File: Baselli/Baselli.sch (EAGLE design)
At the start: 34 parts, among them J2 DF12-ELLI-HEADER-TOP, J3 DF12-ELLI-RECEPTABLE-BOTTOM, J4 FTDI-SER-6-PP, U1 LCMXO2-256HC-4SG32, U2 STM32F051R

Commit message: Change JTAG connector and PIN order for STM32F PB1, PB4 and PB8
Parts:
- removed JP1: (no value), SparkFun-Connectors:M08
- added J5: JTAG_PROG, ELL-i-Connectors:JTAG_PROG
- added Q1: MOSFET-PCHANNELIRLML2244, SparkFun-DiscreteSemi:MOSFET-PCHANNELIRLML2244
- added R12, R13, R14: NP, ELL-i-Passives:R0402
- added R4: 47K, ELL-i-Passives:R0402
- added R9: 10K, ELL-i-Passives:R0402
- R8: value 4K7 (NP) -> 10K
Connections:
- net D3MCU renamed PA11-D3MCU
- net D8MCU renamed PB7-D8MCU
- net N$13 renamed PB10
- net N$14 renamed PB11
- net N$4 renamed PF4
- net N$5 renamed PF5
- removed net N$7: SW1.13, U2PDF.PF6
- removed net N$8: SW1.14, U2PDF.PF7
- new net +5V: J2.5V, J3.5V
- new net N$1: J5.3, Q1.G, R4.2
- new net N$6: J5.7, R14.2
- new net PF6: R13.2, SW1.13, U2PDF.PF6
- new net PF7: R12.2, SW1.14, U2PDF.PF7
- new net VIN: J2.VIN, J3.VIN
- net +3V3: now also J2.VCC(IO), J3.VCC(IO), J5.1, Q1.S, R12.1, R4.1, R9.1; no longer JP1.8
- net D10: now also J5.6; no longer JP1.5
- net D5: now also U2PB.PB1-ADC_IN9; no longer U2PB.PB4
- net D7: now also U2PB.PB8; no longer U2PB.PB1-ADC_IN9
- net GNDI: now also J5.5, J5.9, R13.1, R14.1; no longer JP1.1
- net JTAGENB: now also Q1.D, U2PB.PB4; no longer JP1.6, U2PB.PB8
- net JTDI: now also J5.8; no longer JP1.4
- net NRES: now also J5.10; no longer JP1.7
- net SWCLK: now also J5.4; no longer JP1.3
- net SWDIO: now also J5.2, R9.2; no longer JP1.2
- net VDDA: now also J2.AREF, J3.AREF
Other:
- note added: "In STM32F072 TQFP100, PF6 and PF7 pins are used for GND and VCCIO"
- note removed: "PLACEHOLDER"
- moved on the sheet: R34, R35, R5, R6, R7, R8, SW1, SW2, U1ERB, U1IO, U2PA, U2PB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

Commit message: Adding WS2812B to Baselli board schematics
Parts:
- added D1: (no value), SparkFun-LED:WS2812B
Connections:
- new net PA7: D1.DIN, U2PA.PA7-ADC_IN7
- net +5V: now also D1.VDD
- net GNDI: now also D1.VSS
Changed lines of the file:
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@@
 <?xml version="1.0" encoding="utf-8"?>
 <!DOCTYPE eagle SYSTEM "eagle.dtd">
-<eagle version="6.5.2">
+<eagle version="6.5.0">
 <drawing>
 <settings>
@@
 <part name="R13" library="ELL-i-Passives" deviceset="R" device="0402" value="NP"/>
 <part name="R14" library="ELL-i-Passives" deviceset="R" device="0402" value="NP"/>
+<part name="D1" library="SparkFun-LED" deviceset="WS2812B" device=""/>
+<part name="GNDI15" library="supply1" deviceset="GNDI" device=""/>
+<part name="P+2" library="supply1" deviceset="+5V" device=""/>
 </parts>
 <sheets>
@@
 <instance part="R13" gate="G$1" x="33.02" y="58.42"/>
 <instance part="R14" gate="G$1" x="261.62" y="55.88" rot="R90"/>
+<instance part="D1" gate="G$1" x="-76.2" y="50.8"/>
+<instance part="GNDI15" gate="G$1" x="-53.34" y="43.18"/>
+<instance part="P+2" gate="1" x="-88.9" y="63.5"/>
 </instances>
 <busses>
@@
 <wire x1="15.24" y1="58.42" x2="27.94" y2="58.42" width="0.1524" layer="91"/>
 </segment>
+<segment>
+<pinref part="D1" gate="G$1" pin="VSS"/>
+<pinref part="GNDI15" gate="G$1" pin="GNDI"/>
+<wire x1="-58.42" y1="48.26" x2="-53.34" y2="48.26" width="0.1524" layer="91"/>
+<wire x1="-53.34" y1="48.26" x2="-53.34" y2="45.72" width="0.1524" layer="91"/>
+</segment>
 </net>
 <net name="A0" class="0">
@@
 <label x="91.44" y="325.12" size="1.778" layer="95" xref="yes"/>
 </segment>
+<segment>
+<pinref part="D1" gate="G$1" pin="VDD"/>
+<wire x1="-81.28" y1="55.88" x2="-88.9" y2="55.88" width="0.1524" layer="91"/>
+<wire x1="-88.9" y1="55.88" x2="-88.9" y2="60.96" width="0.1524" layer="91"/>
+<pinref part="P+2" gate="1" pin="+5V"/>
+</segment>
 </net>
 <net name="VIN" class="0">
@@
 </segment>
 </net>
+<net name="PA7" class="0">
+<segment>
+<pinref part="U2" gate="PA" pin="PA7-ADC_IN7"/>
+<wire x1="73.66" y1="154.94" x2="86.36" y2="154.94" width="0.1524" layer="91"/>
+<label x="83.82" y="154.94" size="1.27" layer="95"/>
+</segment>
+<segment>
+<pinref part="D1" gate="G$1" pin="DIN"/>
+<wire x1="-58.42" y1="55.88" x2="-50.8" y2="55.88" width="0.1524" layer="91"/>
+<label x="-53.34" y="55.88" size="1.27" layer="95"/>
+</segment>
+</net>

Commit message: Adding WS2812B RGB LED to Baselli. Begining Arduelli schematic
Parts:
- added TP1: TEST_POINT-5000, ELL-i-Passives:TEST_POINT-5000
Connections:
- new net N$2: D1.DOUT, TP1.P$1
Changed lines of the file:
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@@
 <part name="GNDI15" library="supply1" deviceset="GNDI" device=""/>
 <part name="P+2" library="supply1" deviceset="+5V" device=""/>
+<part name="TP1" library="ELL-i-Passives" deviceset="TEST_POINT" device="-5000"/>
 </parts>
 <sheets>
@@
 <instance part="GNDI15" gate="G$1" x="-53.34" y="43.18"/>
 <instance part="P+2" gate="1" x="-88.9" y="63.5"/>
+<instance part="TP1" gate="TP$1" x="-88.9" y="45.72"/>
 </instances>
 <busses>
@@
 </segment>
 </net>
-<net name="+5V" class="0">
+<net name="+5V" class="1">
 <segment>
 <pinref part="J3" gate="E" pin="5V"/>
@@
 <net name="PA7" class="0">
 <segment>
-<pinref part="U2" gate="PA" pin="PA7-ADC_IN7"/>
-<wire x1="73.66" y1="154.94" x2="86.36" y2="154.94" width="0.1524" layer="91"/>
-<label x="83.82" y="154.94" size="1.27" layer="95"/>
-</segment>
-<segment>
 <pinref part="D1" gate="G$1" pin="DIN"/>
 <wire x1="-58.42" y1="55.88" x2="-50.8" y2="55.88" width="0.1524" layer="91"/>
-<label x="-53.34" y="55.88" size="1.27" layer="95"/>
-</segment>
-</net>
+<label x="-50.8" y="55.88" size="1.778" layer="95" xref="yes"/>
+</segment>
+<segment>
+<pinref part="U2" gate="PA" pin="PA7-ADC_IN7"/>
+<wire x1="73.66" y1="154.94" x2="76.2" y2="154.94" width="0.1524" layer="91"/>
+<label x="76.2" y="154.94" size="1.27" layer="95" xref="yes"/>
+</segment>
+</net>
+<net name="N$2" class="0">
+<segment>
+<pinref part="TP1" gate="TP$1" pin="P$1"/>
+<pinref part="D1" gate="G$1" pin="DOUT"/>
+<wire x1="-88.9" y1="48.26" x2="-81.28" y2="48.26" width="0.1524" layer="91"/>
+</segment>
+</net>

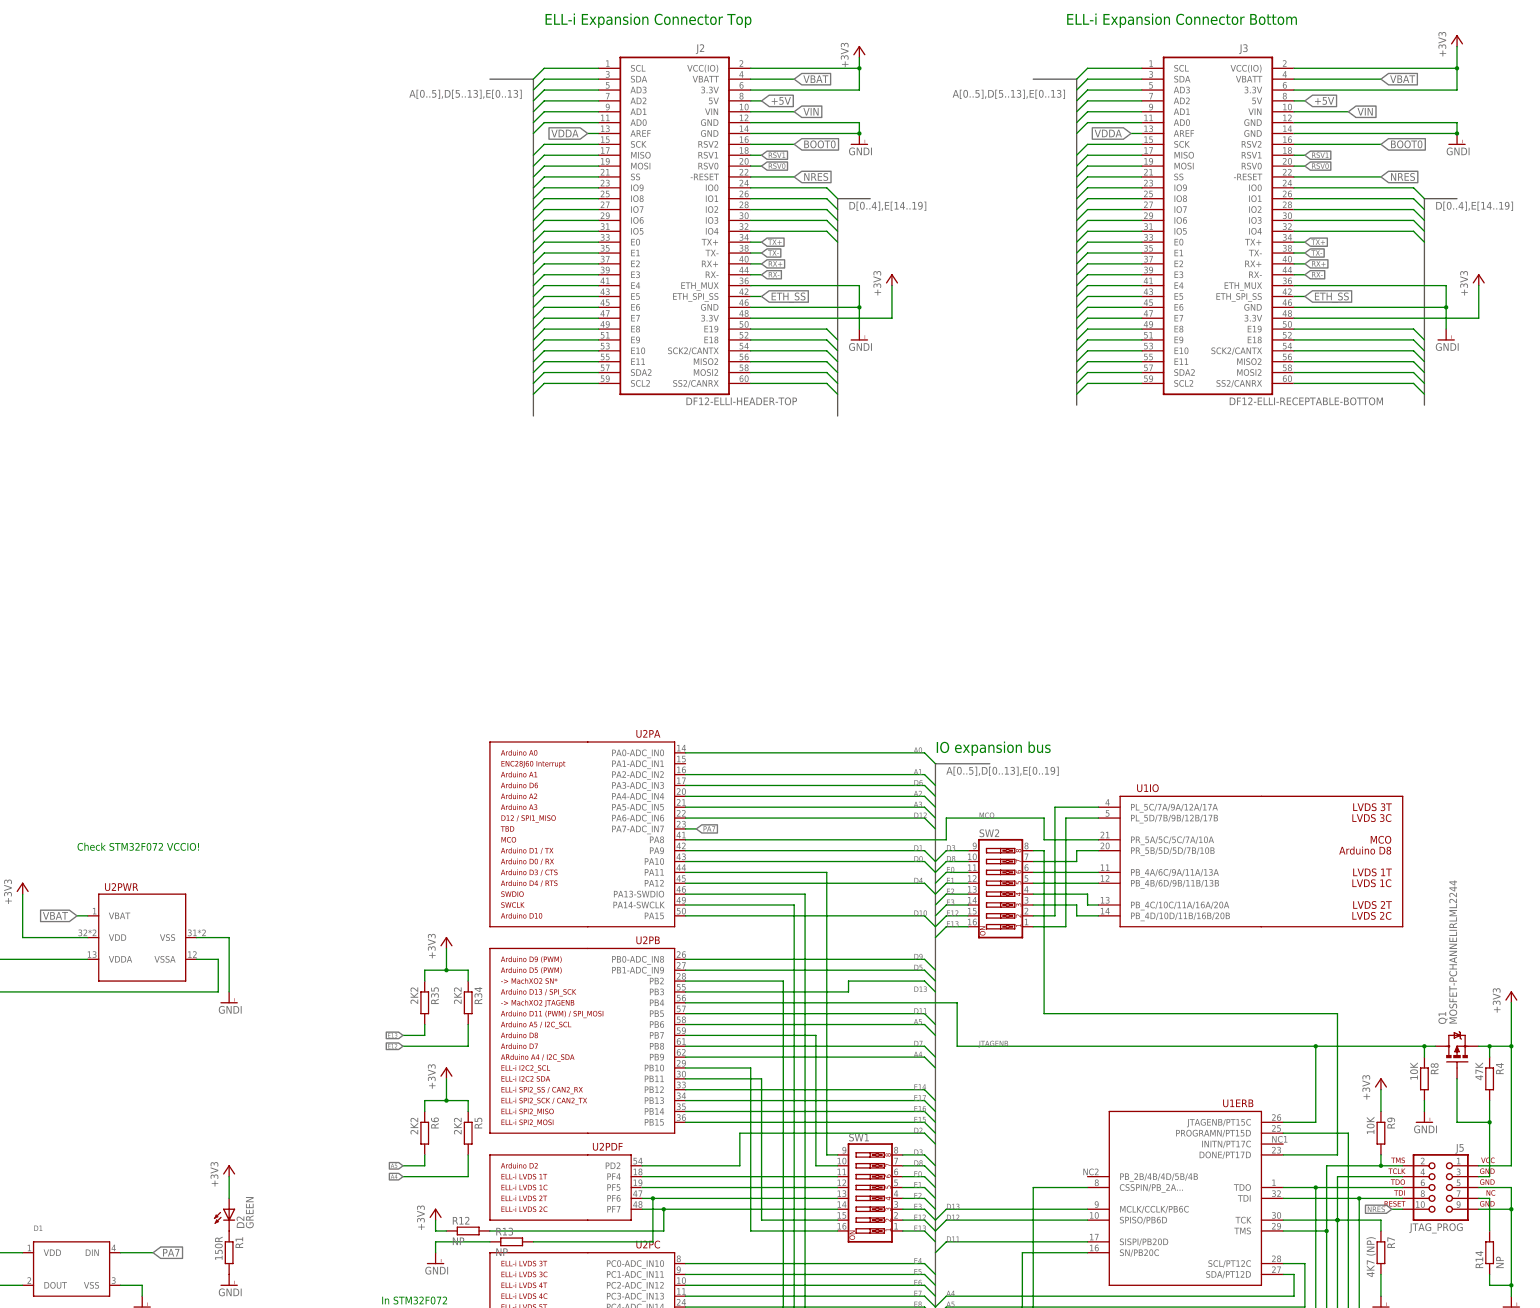
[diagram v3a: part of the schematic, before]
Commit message: Add resistors R10 and R11 to Baselli
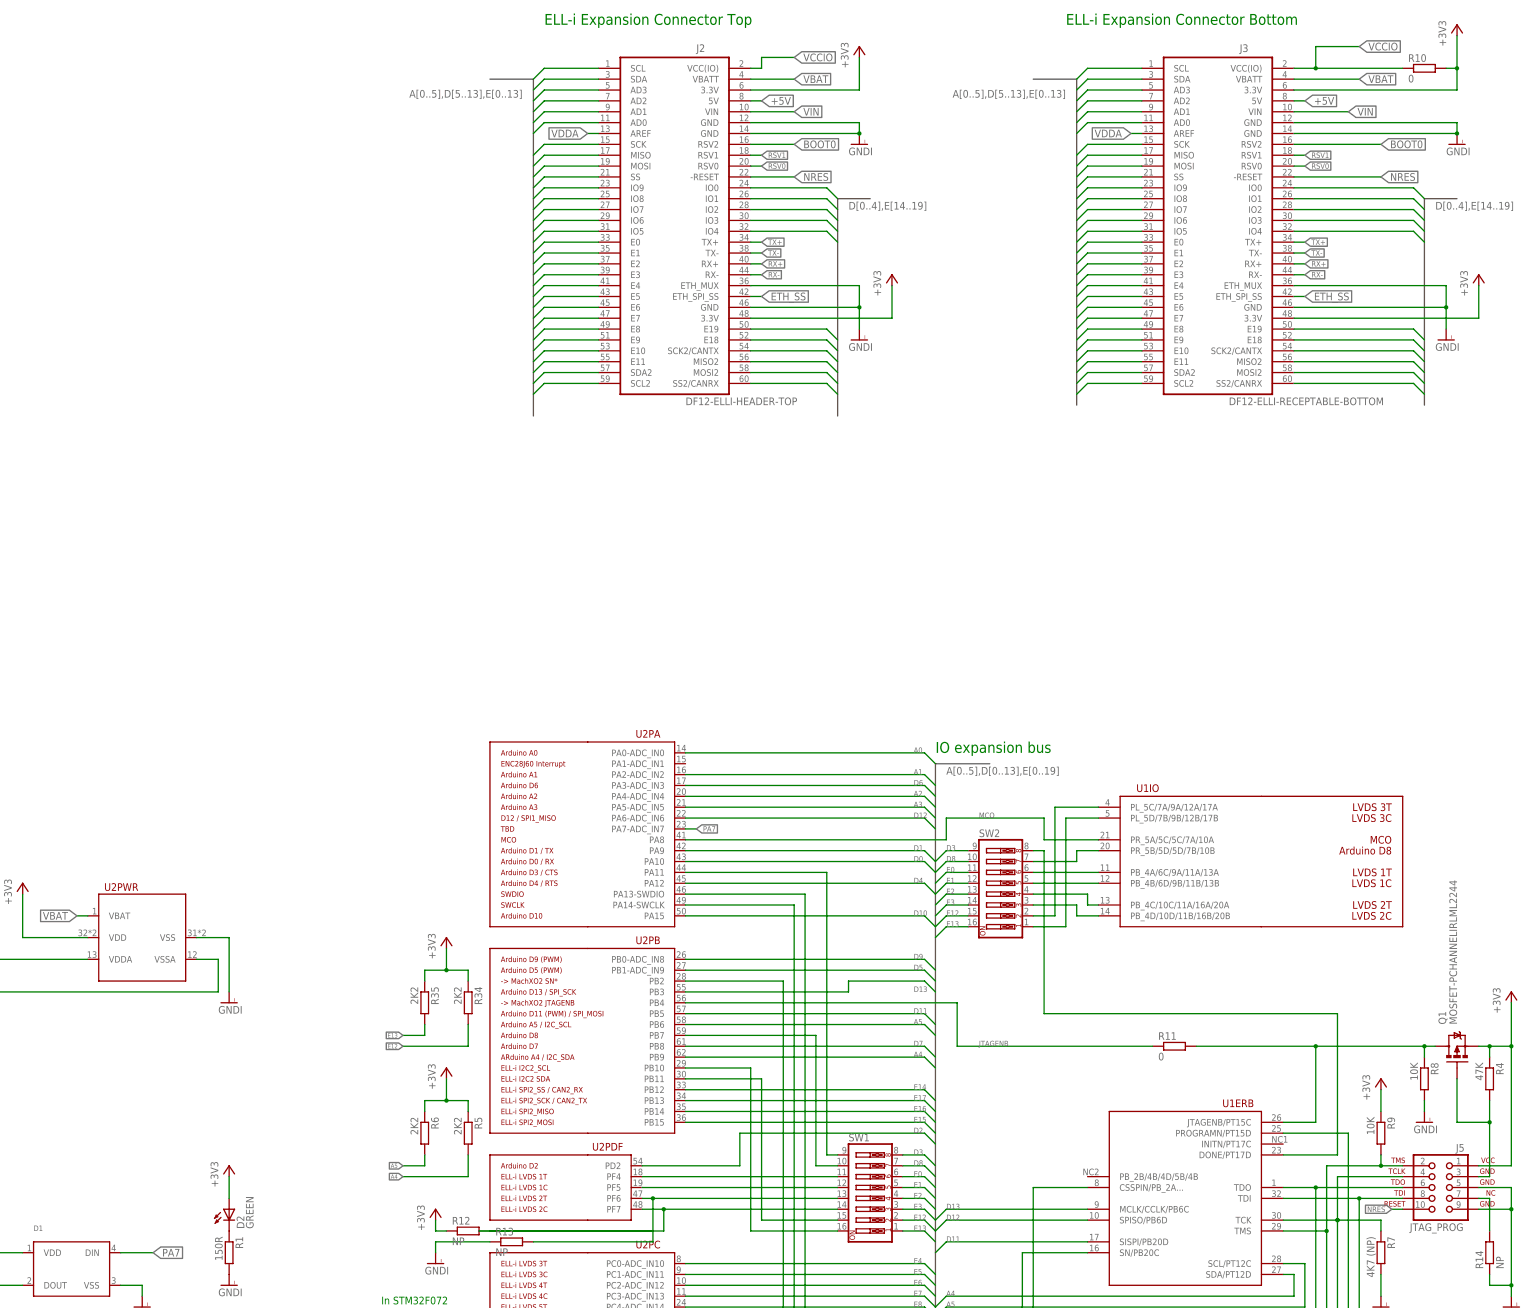
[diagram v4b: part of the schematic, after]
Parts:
- added R10: 0, ELL-i-Passives:R0402
- added R11: 0, ELL-i-Passives:R0805
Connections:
- net N$2 renamed DOUT
- new net JTAGENB$2: Q1.D, R11.2, R8.1, U1ERB.JTAGENB/PT15C
- new net VCCIO: J2.VCC(IO), J3.VCC(IO), R10.1
- net +3V3: now also R10.2; no longer J2.VCC(IO), J3.VCC(IO)
- net JTAGENB: now also R11.1; no longer Q1.D, R8.1, U1ERB.JTAGENB/PT15C
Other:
- note removed: "Check STM32F072 VCCIO!"
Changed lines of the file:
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@@
 <?xml version="1.0" encoding="utf-8"?>
 <!DOCTYPE eagle SYSTEM "eagle.dtd">
-<eagle version="6.5.0">
+<eagle version="6.5.2">
 <drawing>
 <settings>
@@
 <part name="P+2" library="supply1" deviceset="+5V" device=""/>
 <part name="TP1" library="ELL-i-Passives" deviceset="TEST_POINT" device="-5000"/>
+<part name="R10" library="ELL-i-Passives" deviceset="R" device="0402" value="0"/>
+<part name="R11" library="ELL-i-Passives" deviceset="R" device="0805" value="0"/>
 </parts>
 <sheets>
@@
 <text x="40.64" y="342.9" size="2.54" layer="91">ELL-i Expansion Connector Top</text>
 <text x="162.56" y="342.9" size="2.54" layer="91">ELL-i Expansion Connector Bottom</text>
-<text x="-68.58" y="149.86" size="1.778" layer="91">Check STM32F072 VCCIO!</text>
 <text x="-198.12" y="109.22" size="1.27" layer="91">A diode here?</text>
 <text x="2.54" y="30.48" size="1.778" layer="91">In STM32F072
@@
 <instance part="GNDI5" gate="G$1" x="-134.62" y="50.8"/>
 <instance part="+3V5" gate="G$1" x="114.3" y="337.82"/>
-<instance part="+3V8" gate="G$1" x="254" y="340.36"/>
+<instance part="+3V8" gate="G$1" x="254" y="342.9"/>
 <instance part="GNDI10" gate="G$1" x="114.3" y="314.96"/>
 <instance part="GNDI11" gate="G$1" x="254" y="314.96"/>
@@
 <instance part="P+2" gate="1" x="-88.9" y="63.5"/>
 <instance part="TP1" gate="TP$1" x="-88.9" y="45.72"/>
+<instance part="R10" gate="G$1" x="246.38" y="332.74"/>
+<instance part="R11" gate="G$1" x="187.96" y="104.14"/>
 </instances>
 <busses>
@@
 <segment>
 <pinref part="+3V8" gate="G$1" pin="+3V3"/>
-<wire x1="254" y1="337.82" x2="254" y2="332.74" width="0.1524" layer="91"/>
+<wire x1="254" y1="340.36" x2="254" y2="332.74" width="0.1524" layer="91"/>
 <wire x1="254" y1="332.74" x2="254" y2="327.66" width="0.1524" layer="91"/>
 <wire x1="254" y1="327.66" x2="215.9" y2="327.66" width="0.1524" layer="91"/>
 <pinref part="J3" gate="E" pin="3.3V@6"/>
-<pinref part="J3" gate="E" pin="VCC(IO)"/>
-<wire x1="215.9" y1="332.74" x2="254" y2="332.74" width="0.1524" layer="91"/>
+<pinref part="R10" gate="G$1" pin="2"/>
+<wire x1="251.46" y1="332.74" x2="254" y2="332.74" width="0.1524" layer="91"/>
 <junction x="254" y="332.74"/>
 </segment>
@@
 <pinref part="+3V5" gate="G$1" pin="+3V3"/>
 <pinref part="J2" gate="E" pin="3.3V@6"/>
-<wire x1="114.3" y1="335.28" x2="114.3" y2="332.74" width="0.1524" layer="91"/>
-<wire x1="114.3" y1="332.74" x2="114.3" y2="327.66" width="0.1524" layer="91"/>
+<wire x1="114.3" y1="335.28" x2="114.3" y2="327.66" width="0.1524" layer="91"/>
 <wire x1="114.3" y1="327.66" x2="88.9" y2="327.66" width="0.1524" layer="91"/>
-<pinref part="J2" gate="E" pin="VCC(IO)"/>
-<wire x1="114.3" y1="332.74" x2="88.9" y2="332.74" width="0.1524" layer="91"/>
-<junction x="114.3" y="332.74"/>
 </segment>
 <segment>
@@
 <net name="JTAGENB" class="0">
 <segment>
-<pinref part="U1" gate="ERB" pin="JTAGENB/PT15C"/>
-<wire x1="137.16" y1="104.14" x2="220.98" y2="104.14" width="0.1524" layer="91"/>
-<wire x1="220.98" y1="104.14" x2="220.98" y2="86.36" width="0.1524" layer="91"/>
-<wire x1="220.98" y1="86.36" x2="213.36" y2="86.36" width="0.1524" layer="91"/>
+<wire x1="137.16" y1="104.14" x2="182.88" y2="104.14" width="0.1524" layer="91"/>
 <label x="142.24" y="104.14" size="1.27" layer="95"/>
-<junction x="220.98" y="104.14"/>
-<wire x1="220.98" y1="104.14" x2="246.38" y2="104.14" width="0.1524" layer="91"/>
-<pinref part="Q1" gate="G$1" pin="D"/>
-<pinref part="R8" gate="G$1" pin="1"/>
-<wire x1="246.38" y1="104.14" x2="248.92" y2="104.14" width="0.1524" layer="91"/>
-<wire x1="246.38" y1="104.14" x2="246.38" y2="101.6" width="0.1524" layer="91"/>
-<junction x="246.38" y="104.14"/>
 <wire x1="137.16" y1="104.14" x2="137.16" y2="114.3" width="0.1524" layer="91"/>
 <pinref part="U2" gate="PB" pin="PB4"/>
 <wire x1="137.16" y1="114.3" x2="73.66" y2="114.3" width="0.1524" layer="91"/>
+<pinref part="R11" gate="G$1" pin="1"/>
 </segment>
 </net>
@@
 <segment>
 <pinref part="J3" gate="E" pin="VBATT"/>
-<wire x1="215.9" y1="330.2" x2="236.22" y2="330.2" width="0.1524" layer="91"/>
-<label x="236.22" y="330.2" size="1.778" layer="95" xref="yes"/>
+<wire x1="215.9" y1="330.2" x2="231.14" y2="330.2" width="0.1524" layer="91"/>
+<label x="231.14" y="330.2" size="1.778" layer="95" xref="yes"/>
 </segment>
 <segment>
@@
 <junction x="68.58" y="66.04"/>
 </segment>
+<segment>
+<wire x1="25.4" y1="60.96" x2="66.04" y2="60.96" width="0.1524" layer="91"/>
+</segment>
 </net>
 <net name="+5V" class="1">
@@
 </segment>
 </net>
-<net name="N$2" class="0">
+<net name="VCCIO" class="0">
+<segment>
+<pinref part="J2" gate="E" pin="VCC(IO)"/>
+<wire x1="88.9" y1="332.74" x2="91.44" y2="332.74" width="0.1524" layer="91"/>
+<wire x1="91.44" y1="332.74" x2="91.44" y2="335.28" width="0.1524" layer="91"/>
+<wire x1="91.44" y1="335.28" x2="99.06" y2="335.28" width="0.1524" layer="91"/>
+<label x="99.06" y="335.28" size="1.778" layer="95" xref="yes"/>
+</segment>
+<segment>
+<pinref part="J3" gate="E" pin="VCC(IO)"/>
+<pinref part="R10" gate="G$1" pin="1"/>
+<wire x1="241.3" y1="332.74" x2="220.98" y2="332.74" width="0.1524" layer="91"/>
+<wire x1="220.98" y1="332.74" x2="215.9" y2="332.74" width="0.1524" layer="91"/>
+<wire x1="220.98" y1="332.74" x2="220.98" y2="337.82" width="0.1524" layer="91"/>
+<junction x="220.98" y="332.74"/>
+<wire x1="220.98" y1="337.82" x2="231.14" y2="337.82" width="0.1524" layer="91"/>
+<label x="231.14" y="337.82" size="1.778" layer="95" xref="yes"/>
+</segment>
+</net>
+<net name="DOUT" class="0">
 <segment>
 <pinref part="TP1" gate="TP$1" pin="P$1"/>
@@
 </segment>
 </net>
+<net name="JTAGENB$2" class="0">
+<segment>
+<pinref part="R8" gate="G$1" pin="1"/>
+<pinref part="Q1" gate="G$1" pin="D"/>
+<wire x1="246.38" y1="104.14" x2="248.92" y2="104.14" width="0.1524" layer="91"/>
+<wire x1="246.38" y1="104.14" x2="246.38" y2="101.6" width="0.1524" layer="91"/>
+<junction x="246.38" y="104.14"/>
+<pinref part="U1" gate="ERB" pin="JTAGENB/PT15C"/>
+<wire x1="220.98" y1="86.36" x2="213.36" y2="86.36" width="0.1524" layer="91"/>
+<wire x1="220.98" y1="104.14" x2="220.98" y2="86.36" width="0.1524" layer="91"/>
+<junction x="220.98" y="104.14"/>
+<wire x1="220.98" y1="104.14" x2="246.38" y2="104.14" width="0.1524" layer="91"/>
+<wire x1="193.04" y1="104.14" x2="220.98" y2="104.14" width="0.1524" layer="91"/>
+<pinref part="R11" gate="G$1" pin="2"/>
+</segment>
+</net>

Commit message: Update libraries & Small changes to Baselli as agreed on March 5
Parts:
- added R15: 10k, ELL-i-Passives:R0805
- R12, R13, R14: device ELL-i-Passives:R0402 -> ELL-i-Passives:R0805
- R7: device ELL-i-Passives:R0402 -> ELL-i-Passives:R0603
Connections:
- net RX+ renamed ETH_RX+
- net RX- renamed ETH_RX-
- removed net TX+: J2.TX+, J3.TX+
- removed net TX-: J2.TX-, J3.TX-
- new net AREF: J2.AREF, J3.AREF, R15.2
- new net ETH_INT: J2.ETH_INT/TX+, J3.ETH_INT/TX+, U2PA.PA1-ADC_IN1
- new net RSV2: J2.RSV2, J3.RSV2
- net BOOT0: now also J2.BOOT0, J3.BOOT0, R33.2, U2CTL.BOOT0; no longer J2.RSV2, J3.RSV2
- net BOOT0TX: no longer R33.2, U2CTL.BOOT0
- net D0: now also J2.RX1/IO0, J3.RX1/IO0; no longer J2.IO0, J3.IO0
- net D1: now also J2.TX1/IO1, J3.TX1/IO1; no longer J2.IO1, J3.IO1
- net E18: now also J2.RX2/E18, J3.RX2/E18; no longer J2.E18, J3.E18
- net E19: now also J2.TX2/E19, J3.TX2/E19; no longer J2.E19, J3.E19
- net ETH_SS: now also J3.ETH_SS/TX-; no longer J2.ETH_SPI_SS, J3.ETH_SPI_SS
- net VDDA: now also R15.1; no longer J2.AREF, J3.AREF
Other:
- note removed: "A diode here?"
- moved on the sheet: R33
